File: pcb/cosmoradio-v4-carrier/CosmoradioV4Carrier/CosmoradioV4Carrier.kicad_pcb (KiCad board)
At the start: 2 copper layers, 100 x 100 mm, 19 parts, among them J1 EC11-L, J2 EC11-R, J3 BTN, J4 NFC, J5 USB-DONGLE, U1A1 DevKitC-L, U1B1 DevKitC-R

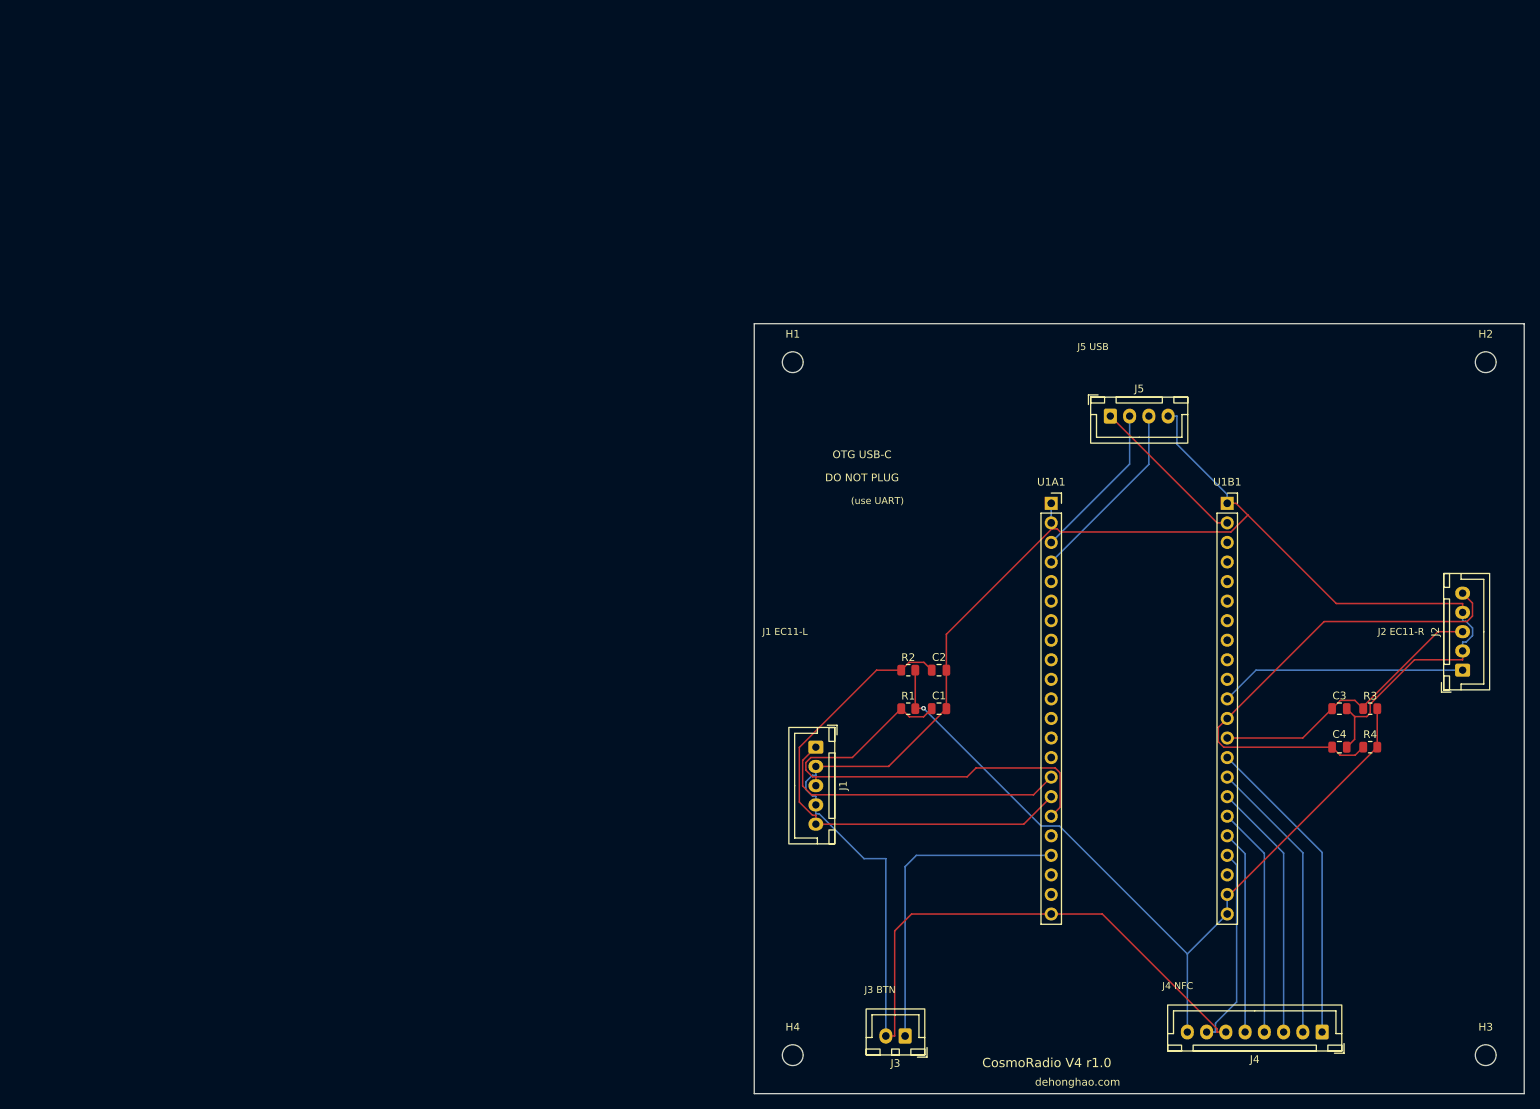
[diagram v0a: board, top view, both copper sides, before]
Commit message: feat(v4): PCB r1.0 实焊验证完成 + 文档 SSOT 重构
PCB r1.0 (JLCEDA Pro 手绘 P1.epro2) 已打板 + 焊接 + 双板并排验证通过。
EC11-R 因 J4 引脚顺序在原理图里画成跟 J3 镜像，物理 EC11 端子线序错位 ——
固件层 walkaround：input_handler.c 重新指派 GPIO_ENC2_A/B/SW 角色，并 swap
A↔B 让两个旋钮"向内拨"方向一致。硬件不返工。

文档执行项目级 SSOT 重构：
- CLAUDE.md "GPIO Pin Assignments" 是 GPIO ↔ net ↔ J pin 的唯一来源
- main/input_handler.c + main/nfc_handler.c 的 #define 是固件 GPIO 角色的
  唯一来源（编译器是 enforcer）
- 其余 9 处文档原本各自维护 GPIO 数字 / J 编号副本，全部清理为指向 CLAUDE.md
  的单行引用；项目特有 GPIO 号 grep 后只在 CLAUDE.md 和 main/*.c 出现

Plan v2 KiCad 备选方案（pcb/cosmoradio-v4-carrier/）housekeeping：
build 脚本拆出 optimize_pcb.py 做布线后处理，重新跑 pcbnew → Freerouting →
Gerber → render，增补 JLCEDA Pro 导出（.eprj2）。状态固化为"备选，未使用"。

Co-Authored-By: Claude Opus 4.7 (1M context) <noreply@anthropic.com>
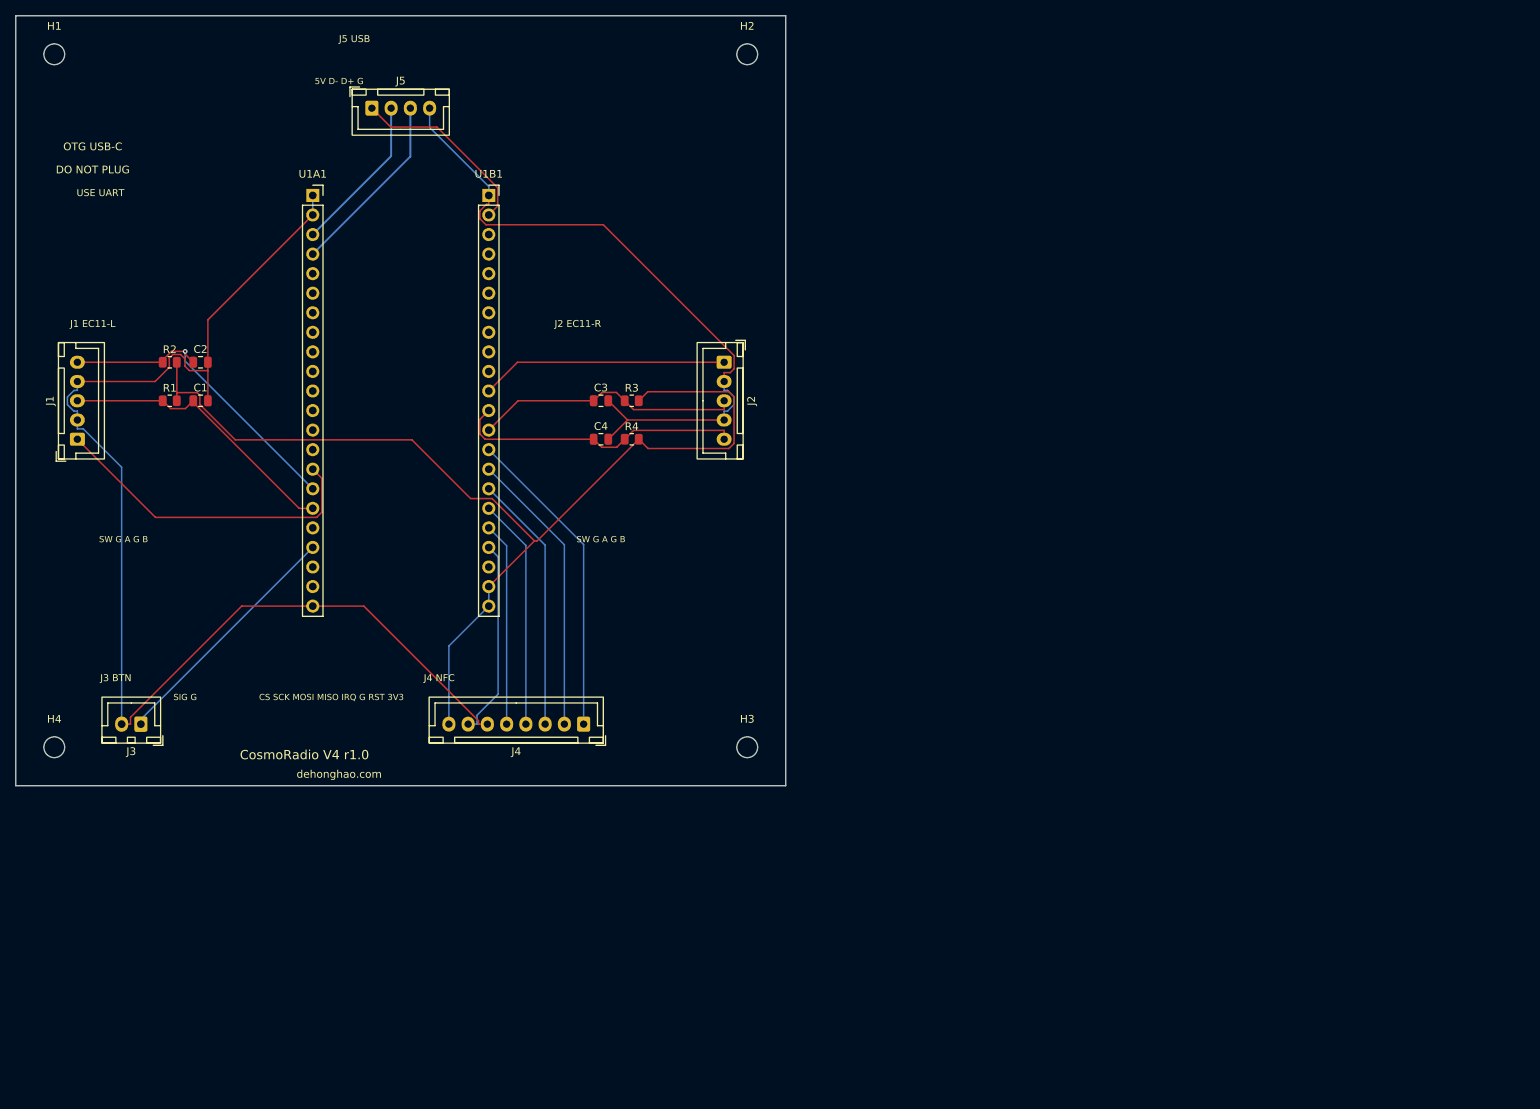
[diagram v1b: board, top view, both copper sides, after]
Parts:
- moved J3 107.2 mm to (16.2, 92.0)
- moved C1 103.9 mm to (24.0, 50.0)
- moved C2 103.9 mm to (24.0, 45.0)
- moved C3 103.9 mm to (76.0, 50.0)
- moved C4 103.9 mm to (76.0, 55.0)
- moved H1 103.9 mm to (5.00, 5.00)
- moved H2 103.9 mm to (95.0, 5.00)
- moved H3 103.9 mm to (95.0, 95.0)
- moved H4 103.9 mm to (5.00, 95.0)
- moved J1 103.9 mm to (8.00, 55.0), turned to 90 degrees
- moved J2 103.9 mm to (92.0, 45.0), turned to -90 degrees
- moved J4 103.9 mm to (73.8, 92.0)
- moved J5 103.9 mm to (46.2, 12.0)
- moved R1 103.9 mm to (20.0, 50.0)
- moved R2 103.9 mm to (20.0, 45.0)
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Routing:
- net 3V3: track 106.0 -> 139.9 mm, vias 1 -> 0
- net ENC2_B: track 64.4 -> 38.0 mm
- net ENC1_A: track 62.5 -> 37.3 mm
- net ENC1_B: track 65.4 -> 41.3 mm, vias 0 -> 1
- net GND: track 270.2 -> 251.9 mm
- net BTN: track 41.6 -> 32.2 mm
- net 5V: track 20.9 -> 24.6 mm
- net ENC1_SW: track 39.5 -> 42.3 mm
- net ENC2_A: track 37.3 -> 34.7 mm
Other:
- board text added: "5V D- D+ G"
- board text added: "CS SCK MOSI MISO IRQ G RST 3V3"
- board text added: "SIG G"
- board text added: "SW G A G B"
- board text added: "USE UART"
- board text removed: "(use UART)"
